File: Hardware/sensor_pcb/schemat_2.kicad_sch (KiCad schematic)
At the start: 40 parts, among them J7 SENSOR_CONN, J8 ToF Sensor

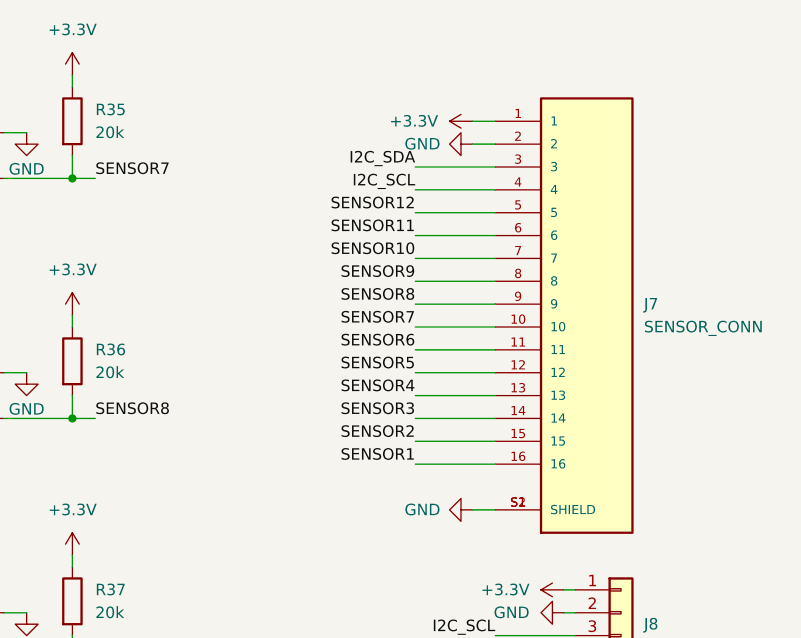
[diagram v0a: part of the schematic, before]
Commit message: PCB sensor layout updated
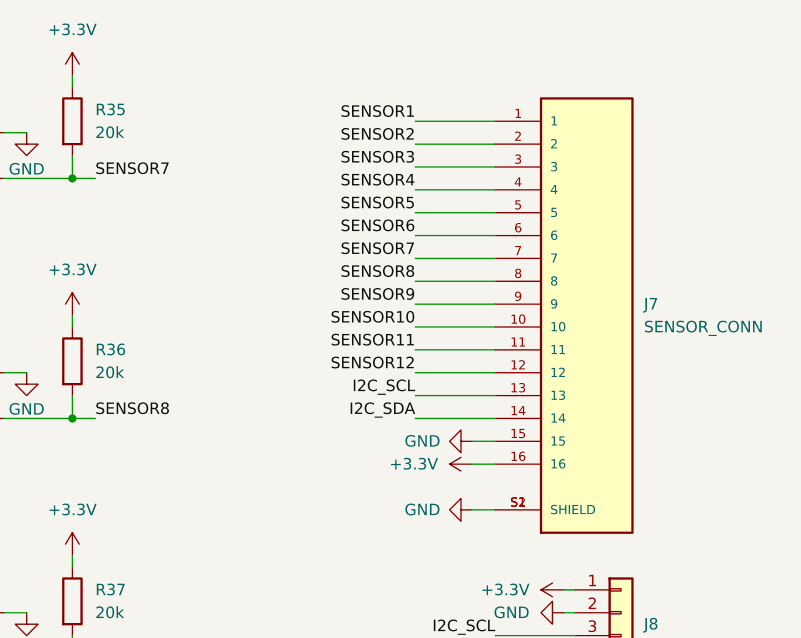
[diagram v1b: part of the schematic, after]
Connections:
- net +3.3V: now also J7.16; no longer J7.1
- net GND: now also J7.15; no longer J7.2
- net I2C_SCL: now also J7.13; no longer J7.4
- net I2C_SDA: now also J7.14; no longer J7.3
- net SENSOR1: now also J7.1; no longer J7.16
- net SENSOR10: now also J7.10; no longer J7.7
- net SENSOR11: now also J7.11; no longer J7.6
- net SENSOR12: now also J7.12; no longer J7.5
- net SENSOR2: now also J7.2; no longer J7.15
- net SENSOR3: now also J7.3; no longer J7.14
- net SENSOR4: now also J7.4; no longer J7.13
- net SENSOR5: now also J7.5; no longer J7.12
- net SENSOR6: now also J7.6; no longer J7.11
- net SENSOR7: now also J7.7; no longer J7.10
- net SENSOR8: now also J7.8; no longer J7.9
- net SENSOR9: now also J7.9; no longer J7.8

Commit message: Minor fixes in schematics, added gerbers and schematics pdfs
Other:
- moved on the sheet: C18, C19, CZ1, CZ10, CZ11, CZ12, CZ2, CZ3, CZ4, CZ5, CZ6, CZ7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
